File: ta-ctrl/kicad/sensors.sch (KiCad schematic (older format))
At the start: 0 parts

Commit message: Added initial pin assignments
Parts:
- added C?: 10uF, symbol pspice:CAP
- added C? (x2): 100nF, symbol pspice:CAP
- added C?: 10nF, symbol pspice:CAP
- added U?: HT-GPS200.20, symbol ta-ctrl:HT-GPS200.20
- added U?: LSM9DS1, Package_LGA:LGA-24L_3x3.5mm_P0.43mm, symbol Sensor_Motion:LSM9DS1
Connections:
- net labels added: GND, SCL, SDA, Vdd, Vdd_GNSS
- wire segments 0 -> 34
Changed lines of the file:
@@
 $Descr A4 11693 8268
 encoding utf-8
-Sheet 1 3
+Sheet 3 3
 Title ""
 Date ""
@@
 Comment4 ""
 $EndDescr
+$Comp
+L ta-ctrl:HT-GPS200.20 U?
+U 1 1 5F242093
+P 3700 5300
+F 0 "U?" H 3675 5715 50  0000 C CNN
+F 1 "HT-GPS200.20" H 3675 5624 50  0000 C CNN
+F 2 "" H 3500 5300 50  0001 C CNN
+F 3 "" H 3500 5300 50  0001 C CNN
+	1    3700 5300
+	1    0    0    -1
+$EndComp
+$Comp
+L Sensor_Motion:LSM9DS1 U?
+U 1 1 5F246320
+P 3700 2500
+F 0 "U?" H 4250 3300 50  0000 C CNN
+F 1 "LSM9DS1" H 3300 1700 50  0000 C CNN
+F 2 "Package_LGA:LGA-24L_3x3.5mm_P0.43mm" H 5200 3250 50  0001 C CNN
+F 3 "http://www.st.com/content/ccc/resource/technical/document/datasheet/1e/3f/2a/d6/25/eb/48/46/DM00103319.pdf/files/DM00103319.pdf/jcr:content/translations/en.DM00103319.pdf" H 3700 2600 50  0001 C CNN
+	1    3700 2500
+	1    0    0    -1
+$EndComp
+Text HLabel 3500 1450 0    50   Input ~ 0
+Vdd
+Text HLabel 2550 5000 0    50   Input ~ 0
+Vdd_GNSS
+Text HLabel 2550 2200 0    50   BiDi ~ 0
+SDA
+Text HLabel 2550 2100 0    50   BiDi ~ 0
+SCL
+Wire Wire Line
+	2550 2100 3000 2100
+Wire Wire Line
+	2550 2200 3000 2200
+$Comp
+L power:GND #PWR?
+U 1 1 5F247619
+P 4550 3100
+F 0 "#PWR?" H 4550 2850 50  0001 C CNN
+F 1 "GND" H 4555 2927 50  0000 C CNN
+F 2 "" H 4550 3100 50  0001 C CNN
+F 3 "" H 4550 3100 50  0001 C CNN
+	1    4550 3100
+	1    0    0    -1
+$EndComp
+Wire Wire Line
+	4550 3000 4550 3100
+Wire Wire Line
+	4400 3000 4550 3000
+Wire Wire Line
+	4400 2900 4550 2900
+Wire Wire Line
+	4550 2900 4550 3000
+Connection ~ 4550 3000
+Wire Wire Line
+	4400 2800 4550 2800
+Wire Wire Line
+	4550 2800 4550 2900
+Connection ~ 4550 2900
+Wire Wire Line
+	4400 2700 4550 2700
+Wire Wire Line
+	4550 2700 4550 2800
+Connection ~ 4550 2800
+Wire Wire Line
+	4400 2600 4550 2600
+Wire Wire Line
+	4550 2600 4550 2700
+Connection ~ 4550 2700
+$Comp
+L power:GND #PWR?
+U 1 1 5F249297
+P 3700 3400
+F 0 "#PWR?" H 3700 3150 50  0001 C CNN
+F 1 "GND" H 3705 3227 50  0000 C CNN
+F 2 "" H 3700 3400 50  0001 C CNN
+F 3 "" H 3700 3400 50  0001 C CNN
+	1    3700 3400
+	1    0    0    -1
+$EndComp
+Wire Wire Line
+	3600 3300 3600 3400
+Wire Wire Line
+	3600 3400 3700 3400
+Wire Wire Line
+	3800 3300 3800 3400
+Wire Wire Line
+	3800 3400 3700 3400
+Connection ~ 3700 3400
+Wire Wire Line
+	3700 1450 3500 1450
+Wire Wire Line
+	3700 1450 3700 1700
+Wire Wire Line
+	3700 1450 3800 1450
+Wire Wire Line
+	3800 1450 3800 1700
+Connection ~ 3700 1450
+Wire Wire Line
+	3800 1450 4000 1450
+Wire Wire Line
+	4000 1450 4000 1700
+Connection ~ 3800 1450
+Wire Wire Line
+	4000 1450 4100 1450
+Wire Wire Line
+	4100 1450 4100 1700
+Connection ~ 4000 1450
+$Comp
+L pspice:CAP C?
+U 1 1 5F24AD8F
+P 5000 1700
+F 0 "C?" H 5178 1746 50  0000 L CNN
+F 1 "10uF" H 5178 1655 50  0000 L CNN
+F 2 "" H 5000 1700 50  0001 C CNN
+F 3 "~" H 5000 1700 50  0001 C CNN
+	1    5000 1700
+	1    0    0    -1
+$EndComp
+$Comp
+L pspice:CAP C?
+U 1 1 5F24C58A
+P 5550 1700
+F 0 "C?" H 5728 1746 50  0000 L CNN
+F 1 "100nF" H 5728 1655 50  0000 L CNN
+F 2 "" H 5550 1700 50  0001 C CNN
+F 3 "~" H 5550 1700 50  0001 C CNN
+	1    5550 1700
+	1    0    0    -1
+$EndComp
+Wire Wire Line
+	4100 1450 5000 1450
+Connection ~ 4100 1450
+Connection ~ 5000 1450
+Wire Wire Line
+	5000 1450 5550 1450
+Wire Wire Line
+	5000 1950 5550 1950
+$Comp
+L power:GND #PWR?
+U 1 1 5F24DC36
+P 5300 2050
+F 0 "#PWR?" H 5300 1800 50  0001 C CNN
+F 1 "GND" H 5305 1877 50  0000 C CNN
+F 2 "" H 5300 2050 50  0001 C CNN
+F 3 "" H 5300 2050 50  0001 C CNN
+	1    5300 2050
+	1    0    0    -1
+$EndComp
+Wire Wire Line
+	5300 1950 5300 2050
+$Comp
+L pspice:CAP C?
+U 1 1 5F24E692
+P 1700 3250
+F 0 "C?" H 1878 3296 50  0000 L CNN
+F 1 "10nF" H 1878 3205 50  0000 L CNN
+F 2 "" H 1700 3250 50  0001 C CNN
+F 3 "~" H 1700 3250 50  0001 C CNN
+	1    1700 3250
+	1    0    0    -1
+$EndComp
+$Comp
+L pspice:CAP C?
+U 1 1 5F24F8D4
+P 2400 3350
+F 0 "C?" H 2578 3396 50  0000 L CNN
+F 1 "100nF" H 2578 3305 50  0000 L CNN
+F 2 "" H 2400 3350 50  0001 C CNN
+F 3 "~" H 2400 3350 50  0001 C CNN
+	1    2400 3350
+	1    0    0    -1
+$EndComp
+Wire Wire Line
+	1700 3000 3000 3000
+Wire Wire Line
+	2400 3100 3000 3100
+Wire Wire Line
+	1700 3500 1700 3600
+Wire Wire Line
+	1700 3600 2050 3600
+$Comp
+L power:GND #PWR?
+U 1 1 5F251C28
+P 2050 3700
+F 0 "#PWR?" H 2050 3450 50  0001 C CNN
+F 1 "GND" H 2055 3527 50  0000 C CNN
+F 2 "" H 2050 3700 50  0001 C CNN
+F 3 "" H 2050 3700 50  0001 C CNN
+	1    2050 3700
+	1    0    0    -1
+$EndComp
+Wire Wire Line
+	2050 3600 2050 3700
+Connection ~ 2050 3600
+Wire Wire Line
+	2050 3600 2400 3600
 $EndSCHEMATC

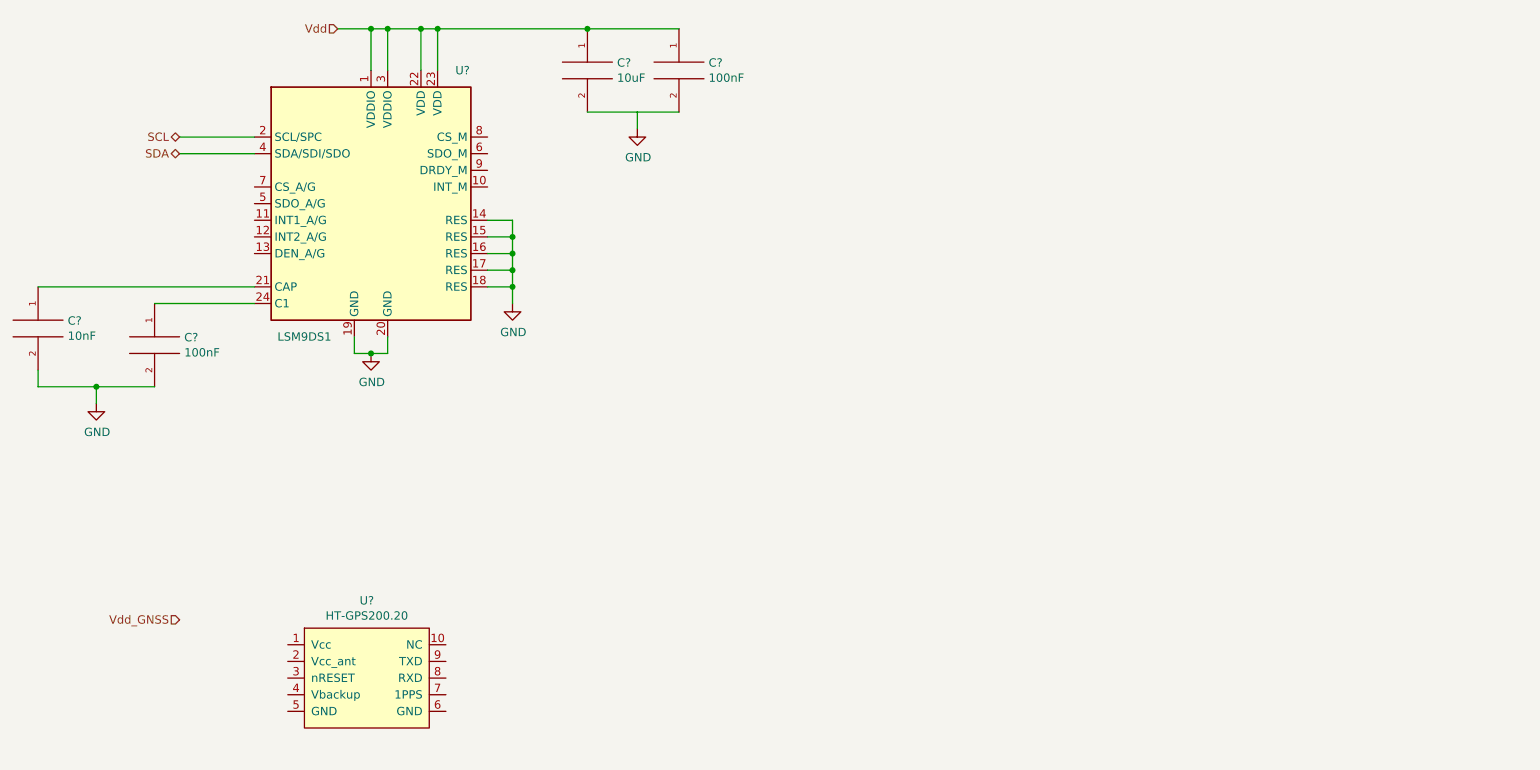
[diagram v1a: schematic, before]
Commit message: level shifters wired in, need to finalize connections between MCU and sensors
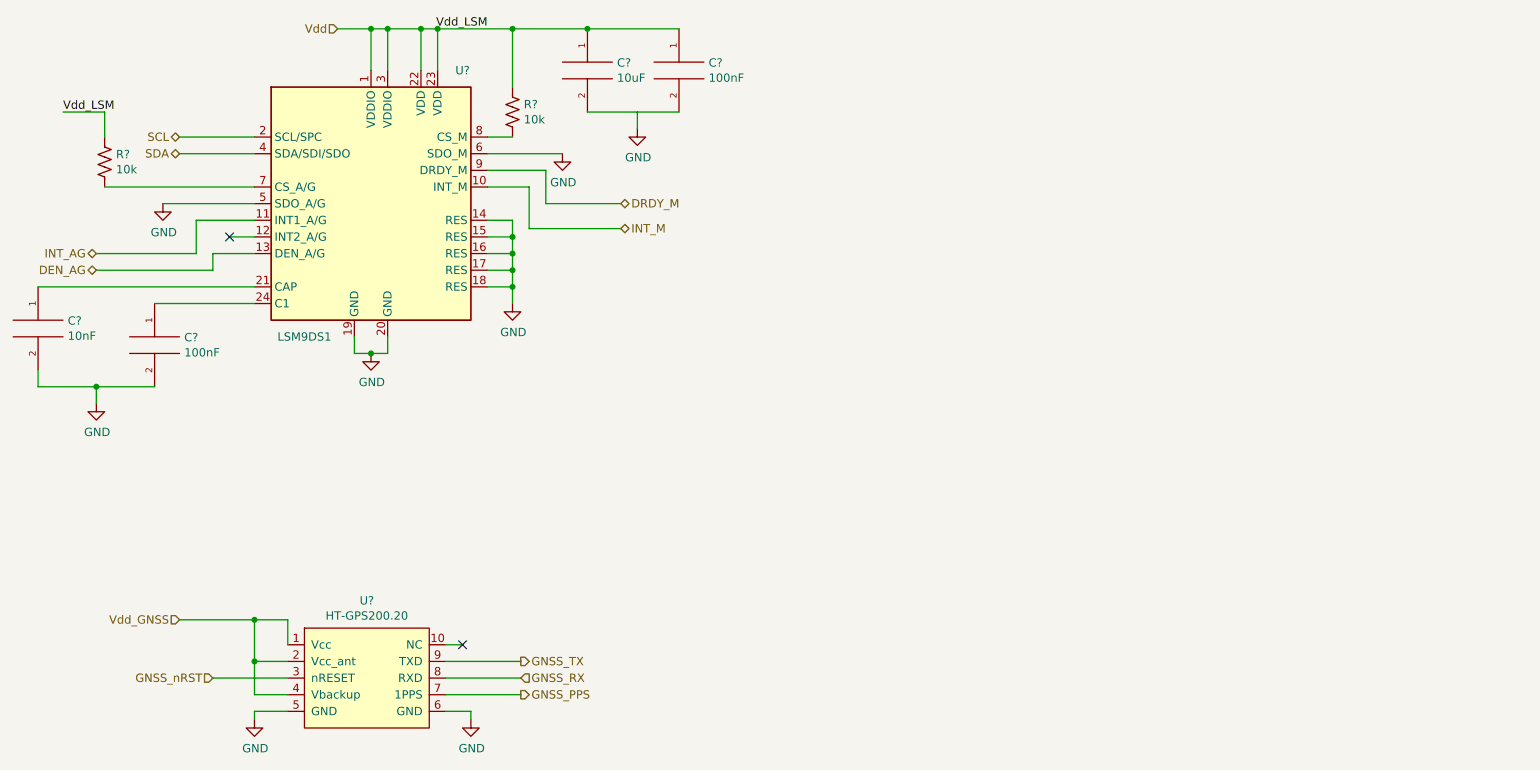
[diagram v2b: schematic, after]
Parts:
- added R? (x2): 10k, symbol Device:R_US
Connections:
- net labels added: DEN_AG, DRDY_M, GNSS_PPS, GNSS_RX, GNSS_TX, GNSS_nRST, INT_AG, INT_M, Vdd_LSM
- wire segments 34 -> 71
- no-connect marks 0 -> 2
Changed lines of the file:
@@
 $EndComp
 Wire Wire Line
-	4100 1450 5000 1450
+	4100 1450 4550 1450
 Connection ~ 4100 1450
 Connection ~ 5000 1450
@@
 Wire Wire Line
 	2050 3600 2400 3600
+$Comp
+L Device:R_US R?
+U 1 1 5F2B2546
+P 4550 1950
+F 0 "R?" H 4618 1996 50  0000 L CNN
+F 1 "10k" H 4618 1905 50  0000 L CNN
+F 2 "" V 4590 1940 50  0001 C CNN
+F 3 "~" H 4550 1950 50  0001 C CNN
+	1    4550 1950
+	1    0    0    -1
+$EndComp
+Wire Wire Line
+	4400 2100 4550 2100
+Wire Wire Line
+	4550 1800 4550 1450
+Connection ~ 4550 1450
+Wire Wire Line
+	4550 1450 5000 1450
+$Comp
+L Device:R_US R?
+U 1 1 5F2B49B6
+P 2100 2250
+F 0 "R?" H 2168 2296 50  0000 L CNN
+F 1 "10k" H 2168 2205 50  0000 L CNN
+F 2 "" V 2140 2240 50  0001 C CNN
+F 3 "~" H 2100 2250 50  0001 C CNN
+	1    2100 2250
+	1    0    0    -1
+$EndComp
+Text Label 4400 1450 2    50   ~ 0
+Vdd_LSM
+Wire Wire Line
+	2100 2400 3000 2400
+Text Label 1850 1950 0    50   ~ 0
+Vdd_LSM
+Wire Wire Line
+	1850 1950 2100 1950
+Wire Wire Line
+	2100 1950 2100 2100
+$Comp
+L power:GND #PWR?
+U 1 1 5F2B83DE
+P 4850 2200
+F 0 "#PWR?" H 4850 1950 50  0001 C CNN
+F 1 "GND" H 4855 2027 50  0000 C CNN
+F 2 "" H 4850 2200 50  0001 C CNN
+F 3 "" H 4850 2200 50  0001 C CNN
+	1    4850 2200
+	1    0    0    -1
+$EndComp
+Wire Wire Line
+	4400 2200 4850 2200
+$Comp
+L power:GND #PWR?
+U 1 1 5F2B9646
+P 2450 2500
+F 0 "#PWR?" H 2450 2250 50  0001 C CNN
+F 1 "GND" H 2455 2327 50  0000 C CNN
+F 2 "" H 2450 2500 50  0001 C CNN
+F 3 "" H 2450 2500 50  0001 C CNN
+	1    2450 2500
+	1    0    0    -1
+$EndComp
+Wire Wire Line
+	2450 2500 3000 2500
+NoConn ~ 2850 2700
+Wire Wire Line
+	2850 2700 3000 2700
+Text HLabel 5200 2500 2    50   BiDi ~ 0
+DRDY_M
+Wire Wire Line
+	4400 2300 4750 2300
+Wire Wire Line
+	4750 2300 4750 2500
+Wire Wire Line
+	4750 2500 5200 2500
+Text HLabel 5200 2650 2    50   BiDi ~ 0
+INT_M
+Wire Wire Line
+	4400 2400 4650 2400
+Wire Wire Line
+	4650 2400 4650 2650
+Wire Wire Line
+	4650 2650 5200 2650
+Wire Wire Line
+	3000 2600 2650 2600
+Wire Wire Line
+	2650 2600 2650 2800
+Wire Wire Line
+	2650 2800 2050 2800
+Wire Wire Line
+	3000 2800 2750 2800
+Wire Wire Line
+	2750 2800 2750 2900
+Wire Wire Line
+	2750 2900 2050 2900
+Text HLabel 2050 2800 0    50   BiDi ~ 0
+INT_AG
+Text HLabel 2050 2900 0    50   BiDi ~ 0
+DEN_AG
+Wire Wire Line
+	2550 5000 3000 5000
+Wire Wire Line
+	3200 5000 3200 5150
+Wire Wire Line
+	3000 5000 3000 5250
+Wire Wire Line
+	3000 5250 3200 5250
+Connection ~ 3000 5000
+Wire Wire Line
+	3000 5000 3200 5000
+Wire Wire Line
+	3000 5250 3000 5450
+Wire Wire Line
+	3000 5450 3200 5450
+Connection ~ 3000 5250
+$Comp
+L power:GND #PWR?
+U 1 1 5F2C42B3
+P 3000 5600
+F 0 "#PWR?" H 3000 5350 50  0001 C CNN
+F 1 "GND" H 3005 5427 50  0000 C CNN
+F 2 "" H 3000 5600 50  0001 C CNN
+F 3 "" H 3000 5600 50  0001 C CNN
+	1    3000 5600
+	1    0    0    -1
+$EndComp
+Wire Wire Line
+	3000 5600 3000 5550
+Wire Wire Line
+	3000 5550 3200 5550
+$Comp
+L power:GND #PWR?
+U 1 1 5F2C6D5D
+P 4300 5600
+F 0 "#PWR?" H 4300 5350 50  0001 C CNN
+F 1 "GND" H 4305 5427 50  0000 C CNN
+F 2 "" H 4300 5600 50  0001 C CNN
+F 3 "" H 4300 5600 50  0001 C CNN
+	1    4300 5600
+	1    0    0    -1
+$EndComp
+Wire Wire Line
+	4150 5550 4300 5550
+Wire Wire Line
+	4300 5550 4300 5600
+NoConn ~ 4250 5150
+Wire Wire Line
+	4150 5150 4250 5150
+Text HLabel 4600 5250 2    50   Output ~ 0
+GNSS_TX
+Wire Wire Line
+	4150 5250 4600 5250
+Text HLabel 4600 5350 2    50   Input ~ 0
+GNSS_RX
+Wire Wire Line
+	4150 5350 4600 5350
+Text HLabel 4600 5450 2    50   Output ~ 0
+GNSS_PPS
+Wire Wire Line
+	4150 5450 4600 5450
+Text HLabel 2750 5350 0    50   Input ~ 0
+GNSS_nRST
+Wire Wire Line
+	2750 5350 3200 5350
 $EndSCHEMATC

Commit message: finalized connections to MCU
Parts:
- added C5: 2.2uF, symbol pspice:CAP
- added R16, R18, R19: DNP, symbol Device:R_US
- gave numbers to parts that had none: 8
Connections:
- net GND: now also C5.2, R16.1, R18.2; no longer U4.5 (SDO_A/G), U4.6 (SDO_M)
- net GNSS_nRST: now also R19.2
- net Vdd_GNSS: now also C5.1, R19.1
- new net: R16.2, U4.5 (SDO_A/G)
- new net: R18.1, U4.6 (SDO_M)
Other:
- moved on the sheet: U5

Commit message: updated and checked all footprints, added a diode too
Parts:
- C1, C2, C3, C4, C5: footprint (none) -> ta-ctrl:C_0603_1608Metric_ctrl_cpy
- R15, R16, R17, R18, R19: footprint (none) -> ta-ctrl:R_0603_1608Metric_ctrl_cpy
- U5: footprint (none) -> ta-ctrl:HT-GPS200.20
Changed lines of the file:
@@
 F 0 "U5" H 9225 3065 50  0000 C CNN
 F 1 "HT-GPS200.20" H 9225 2974 50  0000 C CNN
-F 2 "" H 9050 2650 50  0001 C CNN
+F 2 "ta-ctrl:HT-GPS200.20" H 9050 2650 50  0001 C CNN
 F 3 "" H 9050 2650 50  0001 C CNN
 	1    9250 2650
@@
 Connection ~ 4550 2700
 $Comp
-L power:GND #PWR011
+L power:GND #PWR012
 U 1 1 5F249297
 P 3700 3400
-F 0 "#PWR011" H 3700 3150 50  0001 C CNN
+F 0 "#PWR012" H 3700 3150 50  0001 C CNN
 F 1 "GND" H 3705 3227 50  0000 C CNN
 F 2 "" H 3700 3400 50  0001 C CNN
@@
 F 0 "C3" H 5178 1746 50  0000 L CNN
 F 1 "10uF" H 5178 1655 50  0000 L CNN
-F 2 "" H 5000 1700 50  0001 C CNN
+F 2 "ta-ctrl:C_0603_1608Metric_ctrl_cpy" H 5000 1700 50  0001 C CNN
 F 3 "~" H 5000 1700 50  0001 C CNN
 	1    5000 1700
@@
 F 0 "C4" H 5728 1746 50  0000 L CNN
 F 1 "100nF" H 5728 1655 50  0000 L CNN
-F 2 "" H 5550 1700 50  0001 C CNN
+F 2 "ta-ctrl:C_0603_1608Metric_ctrl_cpy" H 5550 1700 50  0001 C CNN
 F 3 "~" H 5550 1700 50  0001 C CNN
 	1    5550 1700
@@
 	5000 1950 5550 1950
 $Comp
-L power:GND #PWR014
+L power:GND #PWR015
 U 1 1 5F24DC36
 P 5300 2050
-F 0 "#PWR014" H 5300 1800 50  0001 C CNN
+F 0 "#PWR015" H 5300 1800 50  0001 C CNN
 F 1 "GND" H 5305 1877 50  0000 C CNN
 F 2 "" H 5300 2050 50  0001 C CNN
@@
 F 0 "C1" H 1878 3296 50  0000 L CNN
 F 1 "10nF" H 1878 3205 50  0000 L CNN
-F 2 "" H 1700 3250 50  0001 C CNN
+F 2 "ta-ctrl:C_0603_1608Metric_ctrl_cpy" H 1700 3250 50  0001 C CNN
 F 3 "~" H 1700 3250 50  0001 C CNN
 	1    1700 3250
@@
 F 0 "C2" H 2578 3396 50  0000 L CNN
 F 1 "100nF" H 2578 3305 50  0000 L CNN
-F 2 "" H 2400 3350 50  0001 C CNN
+F 2 "ta-ctrl:C_0603_1608Metric_ctrl_cpy" H 2400 3350 50  0001 C CNN
 F 3 "~" H 2400 3350 50  0001 C CNN
 	1    2400 3350
@@
 	1700 3600 2050 3600
 $Comp
-L power:GND #PWR010
+L power:GND #PWR011
 U 1 1 5F251C28
 P 2050 3700
-F 0 "#PWR010" H 2050 3450 50  0001 C CNN
+F 0 "#PWR011" H 2050 3450 50  0001 C CNN
 F 1 "GND" H 2055 3527 50  0000 C CNN
 F 2 "" H 2050 3700 50  0001 C CNN
@@
 F 0 "R17" H 4618 1996 50  0000 L CNN
 F 1 "10k" H 4618 1905 50  0000 L CNN
-F 2 "" V 4590 1940 50  0001 C CNN
+F 2 "ta-ctrl:R_0603_1608Metric_ctrl_cpy" V 4590 1940 50  0001 C CNN
 F 3 "~" H 4550 1950 50  0001 C CNN
 	1    4550 1950
@@
 F 0 "R15" H 2168 2296 50  0000 L CNN
 F 1 "10k" H 2168 2205 50  0000 L CNN
-F 2 "" V 2140 2240 50  0001 C CNN
+F 2 "ta-ctrl:R_0603_1608Metric_ctrl_cpy" V 2140 2240 50  0001 C CNN
 F 3 "~" H 2100 2250 50  0001 C CNN
 	1    2100 2250
@@
 	2100 1950 2100 2100
 $Comp
-L power:GND #PWR013
+L power:GND #PWR014
 U 1 1 5F2B83DE
 P 5000 2300
-F 0 "#PWR013" H 5000 2050 50  0001 C CNN
+F 0 "#PWR014" H 5000 2050 50  0001 C CNN
 F 1 "GND" H 5005 2127 50  0000 C CNN
 F 2 "" H 5000 2300 50  0001 C CNN
@@
 $EndComp
 $Comp
-L power:GND #PWR09
+L power:GND #PWR010
 U 1 1 5F2B9646
 P 2000 2550
-F 0 "#PWR09" H 2000 2300 50  0001 C CNN
+F 0 "#PWR010" H 2000 2300 50  0001 C CNN
 F 1 "GND" H 2005 2377 50  0000 C CNN
 F 2 "" H 2000 2550 50  0001 C CNN
@@
 Connection ~ 8600 2600
 $Comp
-L power:GND #PWR016
+L power:GND #PWR017
 U 1 1 5F2C42B3
 P 8550 2950
-F 0 "#PWR016" H 8550 2700 50  0001 C CNN
+F 0 "#PWR017" H 8550 2700 50  0001 C CNN
 F 1 "GND" H 8555 2777 50  0000 C CNN
 F 2 "" H 8550 2950 50  0001 C CNN
@@
 	8550 2900 8750 2900
 $Comp
-L power:GND #PWR017
+L power:GND #PWR018
 U 1 1 5F2C6D5D
 P 9850 2950
-F 0 "#PWR017" H 9850 2700 50  0001 C CNN
+F 0 "#PWR018" H 9850 2700 50  0001 C CNN
 F 1 "GND" H 9855 2777 50  0000 C CNN
 F 2 "" H 9850 2950 50  0001 C CNN
@@
 F 0 "C5" H 8028 2196 50  0000 L CNN
 F 1 "2.2uF" H 8028 2105 50  0000 L CNN
-F 2 "" H 7850 2150 50  0001 C CNN
+F 2 "ta-ctrl:C_0603_1608Metric_ctrl_cpy" H 7850 2150 50  0001 C CNN
 F 3 "~" H 7850 2150 50  0001 C CNN
 	1    7850 2150
@@
 F 0 "R19" H 8368 2196 50  0000 L CNN
 F 1 "DNP" H 8368 2105 50  0000 L CNN
-F 2 "" V 8340 2140 50  0001 C CNN
+F 2 "ta-ctrl:R_0603_1608Metric_ctrl_cpy" V 8340 2140 50  0001 C CNN
 F 3 "~" H 8300 2150 50  0001 C CNN
 	1    8300 2150
@@
 F 0 "R18" H 4868 2246 50  0000 L CNN
 F 1 "DNP" H 4868 2155 50  0000 L CNN
-F 2 "" V 4840 2190 50  0001 C CNN
+F 2 "ta-ctrl:R_0603_1608Metric_ctrl_cpy" V 4840 2190 50  0001 C CNN
 F 3 "~" H 4800 2200 50  0001 C CNN
 	1    4800 2200
@@
 F 0 "R16" H 2100 2500 50  0000 L CNN
 F 1 "DNP" H 2050 2400 50  0000 L CNN
-F 2 "" V 2290 2490 50  0001 C CNN
+F 2 "ta-ctrl:R_0603_1608Metric_ctrl_cpy" V 2290 2490 50  0001 C CNN
 F 3 "~" H 2250 2500 50  0001 C CNN
 	1    2250 2500
@@
 	2000 2500 2100 2500
 $Comp
-L power:GND #PWR015
+L power:GND #PWR016
 U 1 1 5F77F24C
 P 7850 2450
-F 0 "#PWR015" H 7850 2200 50  0001 C CNN
+F 0 "#PWR016" H 7850 2200 50  0001 C CNN
 F 1 "GND" H 7855 2277 50  0000 C CNN
 F 2 "" H 7850 2450 50  0001 C CNN
@@
 $EndComp
 $Comp
-L power:GND #PWR012
+L power:GND #PWR013
 U 1 1 5F78F3C5
 P 4550 3100
-F 0 "#PWR012" H 4550 2850 50  0001 C CNN
+F 0 "#PWR013" H 4550 2850 50  0001 C CNN
 F 1 "GND" H 4555 2927 50  0000 C CNN
 F 2 "" H 4550 3100 50  0001 C CNN

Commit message: all parts placed, about halfway through routing
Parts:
- U4: footprint Package_LGA:LGA-24L_3x3.5mm_P0.43mm -> ta-ctrl:LSM9DS1TR
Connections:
- net GND: now also C3.2, C4.2
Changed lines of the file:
@@
 F 0 "U4" H 4250 3300 50  0000 C CNN
 F 1 "LSM9DS1" H 3300 1700 50  0000 C CNN
-F 2 "Package_LGA:LGA-24L_3x3.5mm_P0.43mm" H 5200 3250 50  0001 C CNN
+F 2 "ta-ctrl:LSM9DS1TR" H 5200 3250 50  0001 C CNN
 F 3 "http://www.st.com/content/ccc/resource/technical/document/datasheet/1e/3f/2a/d6/25/eb/48/46/DM00103319.pdf/files/DM00103319.pdf/jcr:content/translations/en.DM00103319.pdf" H 3700 2600 50  0001 C CNN
 	1    3700 2500
@@
 L power:GND #PWR012
 U 1 1 5F249297
-P 3700 3400
-F 0 "#PWR012" H 3700 3150 50  0001 C CNN
-F 1 "GND" H 3705 3227 50  0000 C CNN
-F 2 "" H 3700 3400 50  0001 C CNN
-F 3 "" H 3700 3400 50  0001 C CNN
-	1    3700 3400
+P 3700 3500
+F 0 "#PWR012" H 3700 3250 50  0001 C CNN
+F 1 "GND" H 3705 3327 50  0000 C CNN
+F 2 "" H 3700 3500 50  0001 C CNN
+F 3 "" H 3700 3500 50  0001 C CNN
+	1    3700 3500
 	1    0    0    -1
 $EndComp
@@
 	3600 3300 3600 3400
 Wire Wire Line
-	3600 3400 3700 3400
-Wire Wire Line
 	3800 3300 3800 3400
 Wire Wire Line
 	3800 3400 3700 3400
-Connection ~ 3700 3400
 Wire Wire Line
 	3700 1450 3500 1450
@@
 Wire Wire Line
 	5000 1450 5550 1450
-Wire Wire Line
-	5000 1950 5550 1950
-$Comp
-L power:GND #PWR015
-U 1 1 5F24DC36
-P 5300 2050
-F 0 "#PWR015" H 5300 1800 50  0001 C CNN
-F 1 "GND" H 5305 1877 50  0000 C CNN
-F 2 "" H 5300 2050 50  0001 C CNN
-F 3 "" H 5300 2050 50  0001 C CNN
-	1    5300 2050
-	1    0    0    -1
-$EndComp
-Wire Wire Line
-	5300 1950 5300 2050
 $Comp
 L pspice:CAP C1
@@
 	1    0    0    -1
 $EndComp
+Wire Wire Line
+	5000 1950 5300 1950
+$Comp
+L power:GND #PWR015
+U 1 1 5F24DC36
+P 5300 2050
+F 0 "#PWR015" H 5300 1800 50  0001 C CNN
+F 1 "GND" H 5305 1877 50  0000 C CNN
+F 2 "" H 5300 2050 50  0001 C CNN
+F 3 "" H 5300 2050 50  0001 C CNN
+	1    5300 2050
+	1    0    0    -1
+$EndComp
+Wire Wire Line
+	5300 1950 5300 2050
+Connection ~ 5300 1950
+Wire Wire Line
+	5300 1950 5550 1950
+Wire Wire Line
+	3700 3400 3700 3500
+Wire Wire Line
+	3600 3400 3700 3400
+Connection ~ 3700 3400
 $EndSCHEMATC

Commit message: ground plane in and 99percent of the way there with silk screen
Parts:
- U4: footprint ta-ctrl:LSM9DS1TR -> ta-ctrl:LSM9DS1TRL
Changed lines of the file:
@@
 F 0 "U4" H 4250 3300 50  0000 C CNN
 F 1 "LSM9DS1" H 3300 1700 50  0000 C CNN
-F 2 "ta-ctrl:LSM9DS1TR" H 5200 3250 50  0001 C CNN
+F 2 "ta-ctrl:LSM9DS1TRL" H 5200 3250 50  0001 C CNN
 F 3 "http://www.st.com/content/ccc/resource/technical/document/datasheet/1e/3f/2a/d6/25/eb/48/46/DM00103319.pdf/files/DM00103319.pdf/jcr:content/translations/en.DM00103319.pdf" H 3700 2600 50  0001 C CNN
 	1    3700 2500
